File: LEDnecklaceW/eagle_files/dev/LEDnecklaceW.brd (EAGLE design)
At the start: 65 x 35 mm, 21 parts, among them P1 BU2032SM-BT-GCT

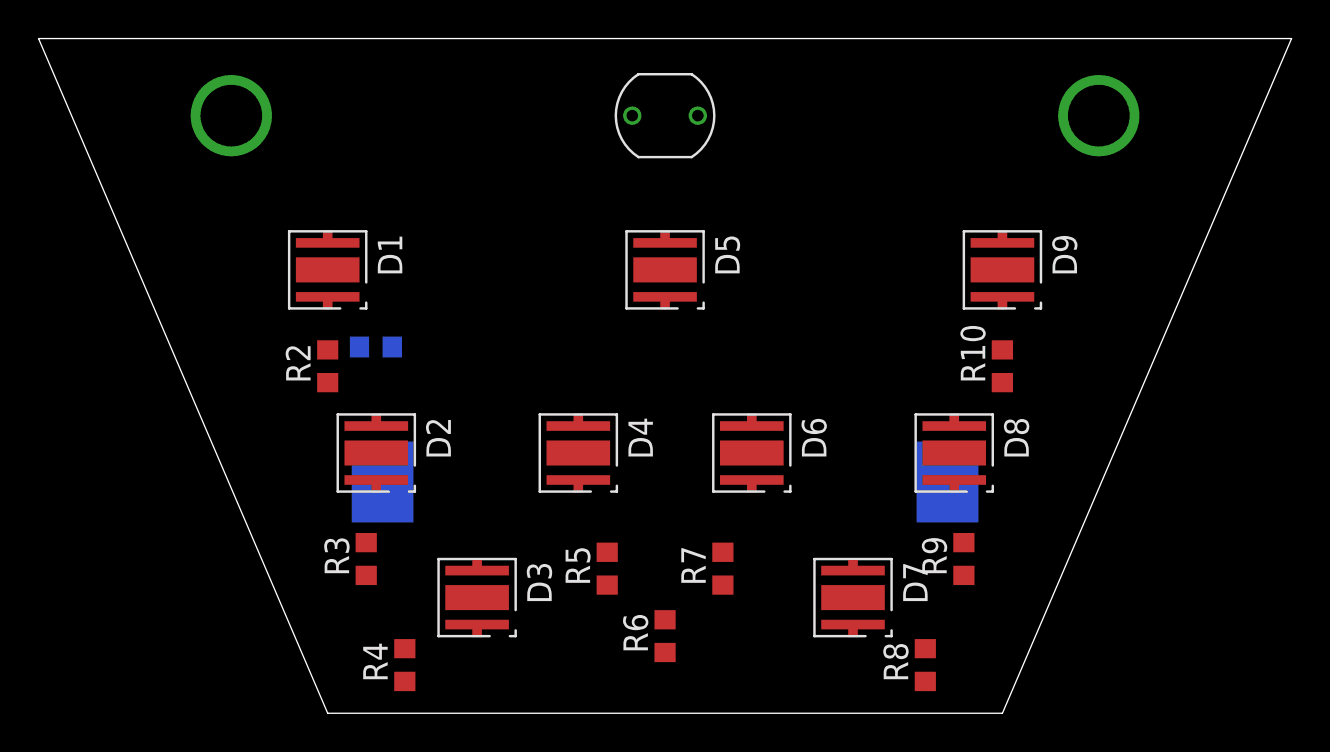
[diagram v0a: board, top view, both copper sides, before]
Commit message: LEDnecklaceW board routed.
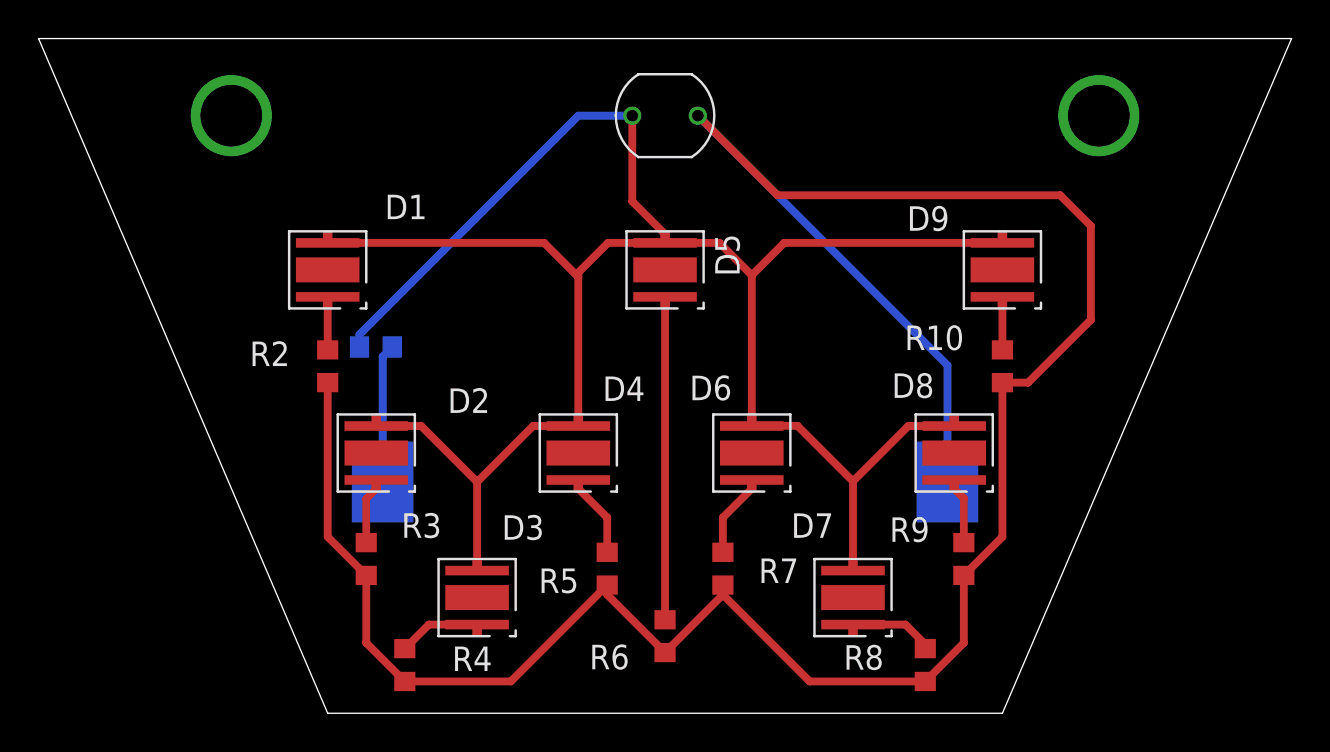
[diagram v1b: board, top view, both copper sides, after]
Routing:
- net N$2: track 0.00 -> 126.7 mm
- net N$15: track 4.05 -> 117.6 mm
- net N$10: track 0.45 -> 16.8 mm
- net N$1: track 0.00 -> 7.21 mm
- net N$12: track 0.45 -> 4.85 mm
- net N$8: track 0.45 -> 4.72 mm
- net N$9: track 0.45 -> 4.37 mm
- net N$11: track 0.45 -> 4.37 mm
- net N$7: track 0.45 -> 3.47 mm
- net N$13: track 0.45 -> 3.46 mm
- net N$5: track 0.45 -> 2.75 mm
- net N$14: track 0.45 -> 2.75 mm

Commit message: LEDnecklaceW board and schematic updated to show component names for photocell and battery.
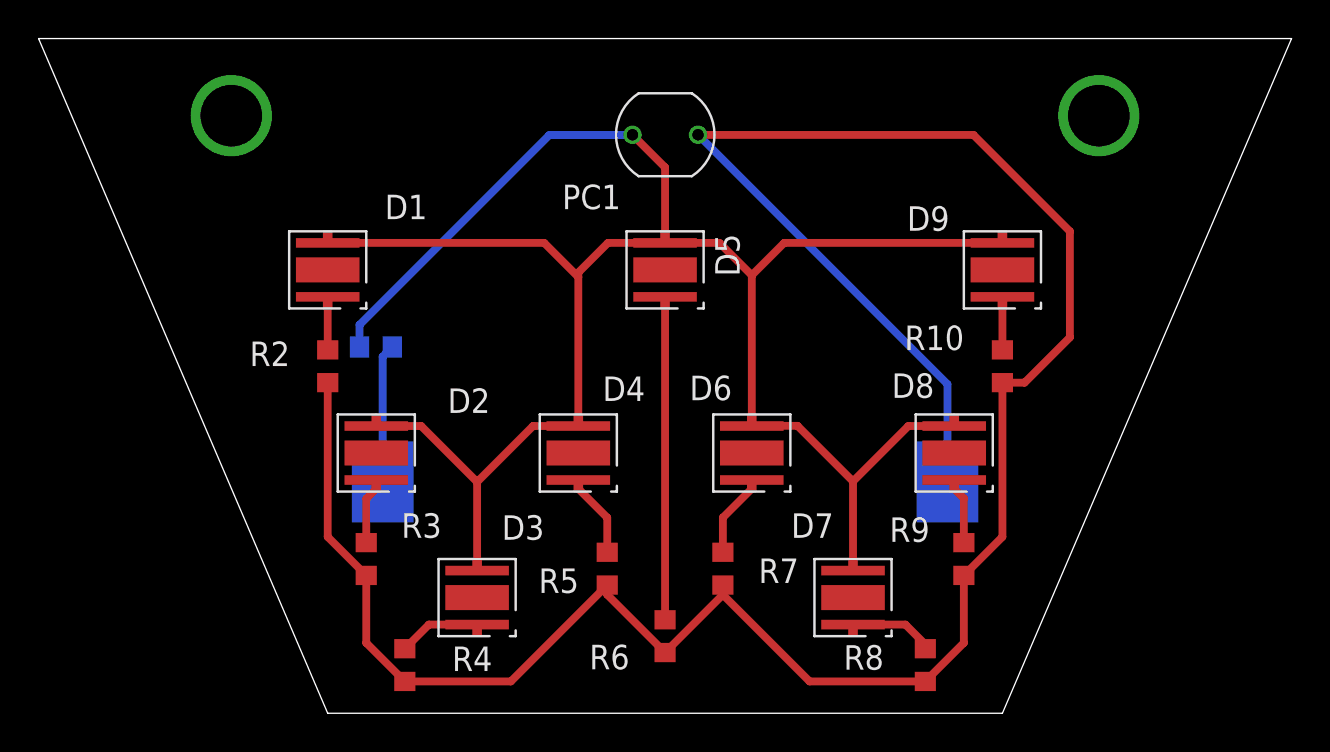
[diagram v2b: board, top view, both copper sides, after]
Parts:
- P1: value BU2032SM-BT-GCT -> (none)
- PC1: value PDV-P8101 -> (none)
- moved PC1 0.99 mm to (17.5, 30.0)
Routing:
- net N$2: track 126.7 -> 123.4 mm
- net N$15: track 117.6 -> 116.5 mm
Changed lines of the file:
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@@
 </autorouter>
 <elements>
-<element name="P1" library="freddyLibr" package="SMD_BATT_HOLDER_2032" value="BU2032SM-BT-GCT" x="17.5" y="12" rot="MR180"/>
 <element name="R1" library="resistor" package="R0603" value="" x="2.5" y="19" smashed="yes" rot="MR180">
 <attribute name="NAME" x="4.811" y="20.971" size="1.27" layer="26" rot="MR180"/>
@@
 <attribute name="VALUE" x="2.032" y="17.111" size="1.27" layer="27" rot="R90"/>
 </element>
-<element name="PC1" library="freddyLibr" package="PHOTOCELL_CERAMIC" value="PDV-P8101" x="17.5" y="31" rot="R90"/>
 <element name="D1" library="freddyLibr" package="SZA05A0A" value="SZA05A0A" x="0" y="23" smashed="yes" rot="R270">
 <attribute name="NAME" x="2.96" y="25.63" size="1.27" layer="21"/>
@@
 <attribute name="VALUE" x="37.032" y="17.111" size="1.27" layer="27" rot="R90"/>
 </element>
+<element name="P1" library="freddyLibr" package="SMD_BATT_HOLDER_2032" value="" x="17.5" y="12" smashed="yes" rot="MR180">
+<attribute name="NAME" x="7.63" y="23.46" size="1.27" layer="26" rot="MR180"/>
+</element>
+<element name="PC1" library="freddyLibr" package="PHOTOCELL_CERAMIC" value="" x="17.51" y="30.01" smashed="yes" rot="R90">
+<attribute name="NAME" x="15.2" y="27.42" size="1.27" layer="25" rot="R180"/>
+</element>
 </elements>
 <signals>
 <signal name="N$1">
+<contactref element="R1" pad="2"/>
 <contactref element="P1" pad="VCC"/>
-<contactref element="R1" pad="2"/>
 <wire x1="2.85" y1="12" x2="2.85" y2="18.5" width="0.4064" layer="16"/>
 <wire x1="2.85" y1="18.5" x2="3.35" y2="19" width="0.4064" layer="16"/>
 </signal>
 <signal name="N$2">
-<contactref element="P1" pad="GND"/>
-<contactref element="PC1" pad="2"/>
 <contactref element="R10" pad="1"/>
 <contactref element="R9" pad="1"/>
@@
 <wire x1="35" y1="17.15" x2="35" y2="9.15" width="0.4064" layer="1"/>
 <wire x1="35" y1="9.15" x2="33" y2="7.15" width="0.4064" layer="1"/>
-<wire x1="35" y1="17.15" x2="36.33" y2="17.15" width="0.4064" layer="1"/>
-<wire x1="36.33" y1="17.15" x2="39.59" y2="20.41" width="0.4064" layer="1"/>
-<wire x1="39.59" y1="20.41" x2="39.59" y2="25.28" width="0.4064" layer="1"/>
-<wire x1="39.59" y1="25.28" x2="38" y2="26.87" width="0.4064" layer="1"/>
-<wire x1="38" y1="26.87" x2="23.33" y2="26.87" width="0.4064" layer="1"/>
-<wire x1="23.33" y1="26.87" x2="19.2" y2="31" width="0.4064" layer="1"/>
-<wire x1="32.15" y1="12" x2="32.15" y2="18.05" width="0.4064" layer="16"/>
-<wire x1="32.15" y1="18.05" x2="19.2" y2="31" width="0.4064" layer="16"/>
+<contactref element="P1" pad="GND"/>
+<contactref element="PC1" pad="2"/>
+<wire x1="32.15" y1="12" x2="32.15" y2="17.07" width="0.4064" layer="16"/>
+<wire x1="32.15" y1="17.07" x2="19.21" y2="30.01" width="0.4064" layer="16"/>
+<wire x1="35" y1="17.15" x2="36.15" y2="17.15" width="0.4064" layer="1"/>
+<wire x1="36.15" y1="17.15" x2="38.5" y2="19.5" width="0.4064" layer="1"/>
+<wire x1="38.5" y1="19.5" x2="38.5" y2="25" width="0.4064" layer="1"/>
+<wire x1="38.5" y1="25" x2="33.5" y2="30" width="0.4064" layer="1"/>
+<wire x1="33.5" y1="30" x2="19.22" y2="30" width="0.4064" layer="1"/>
+<wire x1="19.22" y1="30" x2="19.21" y2="30.01" width="0.4064" layer="1"/>
 </signal>
 <signal name="N$5">
@@
 <signal name="N$15">
 <contactref element="R1" pad="1"/>
-<contactref element="PC1" pad="1"/>
 <contactref element="D9" pad="1"/>
 <contactref element="D9" pad="11"/>
@@
 <wire x1="0" y1="24.4" x2="11.23" y2="24.4" width="0.4064" layer="1"/>
 <wire x1="11.23" y1="24.4" x2="13" y2="22.63" width="0.4064" layer="1"/>
-<wire x1="15.8" y1="31" x2="15.8" y2="26.55" width="0.4064" layer="1"/>
-<wire x1="15.8" y1="26.55" x2="17.5" y2="24.85" width="0.4064" layer="1"/>
-<wire x1="1.65" y1="19" x2="1.65" y2="19.65" width="0.4064" layer="16"/>
-<wire x1="1.65" y1="19.65" x2="13" y2="31" width="0.4064" layer="16"/>
-<wire x1="13" y1="31" x2="15.8" y2="31" width="0.4064" layer="16"/>
+<contactref element="PC1" pad="1"/>
+<wire x1="17.5" y1="24.85" x2="17.5" y2="28.32" width="0.4064" layer="1"/>
+<wire x1="17.5" y1="28.32" x2="15.81" y2="30.01" width="0.4064" layer="1"/>
+<wire x1="1.65" y1="19" x2="1.65" y2="20.15" width="0.4064" layer="16"/>
+<wire x1="1.65" y1="20.15" x2="11.5" y2="30" width="0.4064" layer="16"/>
+<wire x1="11.5" y1="30" x2="15.8" y2="30" width="0.4064" layer="16"/>
+<wire x1="15.8" y1="30" x2="15.81" y2="30.01" width="0.4064" layer="16"/>
 </signal>
 <signal name="N$3">

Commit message: Moved some names around.
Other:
- board size 65 x 35 mm -> 55 x 35 mm
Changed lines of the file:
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@@
 <plain>
 <wire x1="0" y1="0" x2="35" y2="0" width="0" layer="20"/>
-<wire x1="35" y1="0" x2="50" y2="35" width="0" layer="20"/>
-<wire x1="50" y1="35" x2="-15" y2="35" width="0" layer="20"/>
-<wire x1="-15" y1="35" x2="0" y2="0" width="0" layer="20"/>
+<wire x1="35" y1="0" x2="45" y2="35" width="0" layer="20"/>
+<wire x1="45" y1="35" x2="-10" y2="35" width="0" layer="20"/>
+<wire x1="-10" y1="35" x2="0" y2="0" width="0" layer="20"/>
 </plain>
 <attributes>
@@
 </element>
 <element name="R2" library="resistor" package="R0603" value="" x="0" y="18" smashed="yes" rot="R90">
-<attribute name="NAME" x="-1.961" y="19.281" size="1.27" layer="25" rot="R180"/>
+<attribute name="NAME" x="-1.801" y="19.361" size="1.27" layer="25" rot="R180"/>
 <attribute name="VALUE" x="2.032" y="17.111" size="1.27" layer="27" rot="R90"/>
 </element>
@@
 </element>
 <element name="D5" library="freddyLibr" package="SZA05A0A" value="SZA05A0A" x="17.5" y="23" smashed="yes" rot="R270">
-<attribute name="NAME" x="20.1" y="24.87" size="1.27" layer="21" rot="R270"/>
+<attribute name="NAME" x="19.05" y="25.72" size="1.27" layer="21"/>
 </element>
 <element name="D6" library="freddyLibr" package="SZA05A0A" value="SZA05A0A" x="22" y="13.5" smashed="yes" rot="R270">
@@
 </element>
 <element name="R10" library="resistor" package="R0603" value="" x="35" y="18" smashed="yes" rot="R90">
-<attribute name="NAME" x="33.009" y="20.111" size="1.27" layer="25" rot="R180"/>
+<attribute name="NAME" x="32.759" y="20.201" size="1.27" layer="25" rot="R180"/>
 <attribute name="VALUE" x="37.032" y="17.111" size="1.27" layer="27" rot="R90"/>
 </element>

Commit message: Added switch to board and schematic. Also added output production files corresponding to these changes.
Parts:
- added SW1: PCM12SMTR, freddyLibr:PCM12SMTR
- moved R1 7.16 mm to (4.00, 12.0)
- moved P1 6.00 mm to (17.5, 18.0)
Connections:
- new net N$6: P1.VCC, SW1.1
- net N$1: now also SW1.2; no longer P1.VCC
- net N$2: now also SW1.3
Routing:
- net N$6: track 0.00 -> 13.6 mm
- net N$15: track 116.5 -> 129.9 mm
- net N$2: track 123.4 -> 136.3 mm
- net N$1: track 7.21 -> 20.0 mm
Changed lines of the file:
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@@
 </autorouter>
 <elements>
-<element name="R1" library="resistor" package="R0603" value="" x="2.5" y="19" smashed="yes" rot="MR180">
-<attribute name="NAME" x="4.811" y="20.971" size="1.27" layer="26" rot="MR180"/>
-<attribute name="VALUE" x="1.611" y="21.032" size="1.27" layer="28" rot="MR180"/>
+<element name="R1" library="resistor" package="R0603" value="" x="4" y="12" smashed="yes" rot="MR180">
+<attribute name="NAME" x="0.491" y="10.401" size="1.27" layer="26" rot="MR180"/>
+<attribute name="VALUE" x="3.111" y="14.032" size="1.27" layer="28" rot="MR180"/>
 </element>
 <element name="R2" library="resistor" package="R0603" value="" x="0" y="18" smashed="yes" rot="R90">
@@
 <attribute name="VALUE" x="37.032" y="17.111" size="1.27" layer="27" rot="R90"/>
 </element>
-<element name="P1" library="freddyLibr" package="SMD_BATT_HOLDER_2032" value="" x="17.5" y="12" smashed="yes" rot="MR180">
-<attribute name="NAME" x="7.63" y="23.46" size="1.27" layer="26" rot="MR180"/>
+<element name="P1" library="freddyLibr" package="SMD_BATT_HOLDER_2032" value="" x="17.5" y="18" smashed="yes" rot="MR180">
+<attribute name="NAME" x="25.7" y="28.29" size="1.27" layer="26" rot="MR180"/>
 </element>
 <element name="PC1" library="freddyLibr" package="PHOTOCELL_CERAMIC" value="" x="17.51" y="30.01" smashed="yes" rot="R90">
 <attribute name="NAME" x="15.2" y="27.42" size="1.27" layer="25" rot="R180"/>
 </element>
+<element name="SW1" library="freddyLibr" package="PCM12SMTR" value="PCM12SMTR" x="6" y="32.99" smashed="yes" rot="MR180">
+<attribute name="NAME" x="-1.79" y="30.16" size="1.27" layer="26" rot="MR180"/>
+</element>
 </elements>
 <signals>
-<signal name="N$1">
-<contactref element="R1" pad="2"/>
-<contactref element="P1" pad="VCC"/>
-<wire x1="2.85" y1="12" x2="2.85" y2="18.5" width="0.4064" layer="16"/>
-<wire x1="2.85" y1="18.5" x2="3.35" y2="19" width="0.4064" layer="16"/>
-</signal>
 <signal name="N$2">
 <contactref element="R10" pad="1"/>
@@
 <contactref element="P1" pad="GND"/>
 <contactref element="PC1" pad="2"/>
-<wire x1="32.15" y1="12" x2="32.15" y2="17.07" width="0.4064" layer="16"/>
-<wire x1="32.15" y1="17.07" x2="19.21" y2="30.01" width="0.4064" layer="16"/>
 <wire x1="35" y1="17.15" x2="36.15" y2="17.15" width="0.4064" layer="1"/>
 <wire x1="36.15" y1="17.15" x2="38.5" y2="19.5" width="0.4064" layer="1"/>
@@
 <wire x1="33.5" y1="30" x2="19.22" y2="30" width="0.4064" layer="1"/>
 <wire x1="19.22" y1="30" x2="19.21" y2="30.01" width="0.4064" layer="1"/>
+<contactref element="SW1" pad="3"/>
+<wire x1="32.15" y1="18" x2="32.15" y2="27.62" width="0.4064" layer="16"/>
+<wire x1="32.15" y1="27.62" x2="29.77" y2="30" width="0.4064" layer="16"/>
+<wire x1="29.77" y1="30" x2="19.22" y2="30" width="0.4064" layer="16"/>
+<wire x1="19.22" y1="30" x2="19.21" y2="30.01" width="0.4064" layer="16"/>
+<wire x1="19.21" y1="30.01" x2="19.21" y2="30.13" width="0.4064" layer="16"/>
+<wire x1="19.21" y1="30.13" x2="17.93" y2="31.41" width="0.4064" layer="16"/>
+<wire x1="17.93" y1="31.41" x2="12.7" y2="31.41" width="0.4064" layer="16"/>
+<wire x1="12.7" y1="31.41" x2="11.32" y2="30.03" width="0.4064" layer="16"/>
+<wire x1="11.32" y1="30.03" x2="9.46" y2="30.03" width="0.4064" layer="16"/>
+<wire x1="9.46" y1="30.03" x2="8.25" y2="31.24" width="0.4064" layer="16"/>
 </signal>
 <signal name="N$5">
@@
 <wire x1="17.5" y1="24.85" x2="17.5" y2="28.32" width="0.4064" layer="1"/>
 <wire x1="17.5" y1="28.32" x2="15.81" y2="30.01" width="0.4064" layer="1"/>
-<wire x1="1.65" y1="19" x2="1.65" y2="20.15" width="0.4064" layer="16"/>
-<wire x1="1.65" y1="20.15" x2="11.5" y2="30" width="0.4064" layer="16"/>
-<wire x1="11.5" y1="30" x2="15.8" y2="30" width="0.4064" layer="16"/>
-<wire x1="15.8" y1="30" x2="15.81" y2="30.01" width="0.4064" layer="16"/>
+<wire x1="3.15" y1="12" x2="3.15" y2="11.64" width="0.4064" layer="16"/>
+<wire x1="3.15" y1="11.64" x2="4.99" y2="9.8" width="0.4064" layer="16"/>
+<wire x1="4.99" y1="9.8" x2="13.55" y2="9.8" width="0.4064" layer="16"/>
+<wire x1="13.55" y1="9.8" x2="15.98" y2="12.23" width="0.4064" layer="16"/>
+<wire x1="15.98" y1="12.23" x2="15.98" y2="29.84" width="0.4064" layer="16"/>
+<wire x1="15.98" y1="29.84" x2="15.81" y2="30.01" width="0.4064" layer="16"/>
 </signal>
 <signal name="N$3">
@@
 <via x="40" y="31" extent="1-16" drill="3.2" diameter="2.54"/>
 </signal>
+<signal name="N$1">
+<contactref element="R1" pad="2"/>
+<contactref element="SW1" pad="2"/>
+<wire x1="6.75" y1="31.24" x2="6.75" y2="13.9" width="0.4064" layer="16"/>
+<wire x1="6.75" y1="13.9" x2="4.85" y2="12" width="0.4064" layer="16"/>
+</signal>
+<signal name="N$6">
+<contactref element="P1" pad="VCC"/>
+<contactref element="SW1" pad="1"/>
+<wire x1="2.85" y1="18" x2="2.85" y2="30.34" width="0.4064" layer="16"/>
+<wire x1="2.85" y1="30.34" x2="3.75" y2="31.24" width="0.4064" layer="16"/>
+</signal>
 </signals>
